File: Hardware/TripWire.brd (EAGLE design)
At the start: 32.3 x 50.2 mm, 69 parts, among them P1 LSP11, P2 LSP11, P3 LSP11, P4 LSP11, P5 LSP11, P6 LSP11, P7 LSP11, X1 GADGETEER-SOCKET

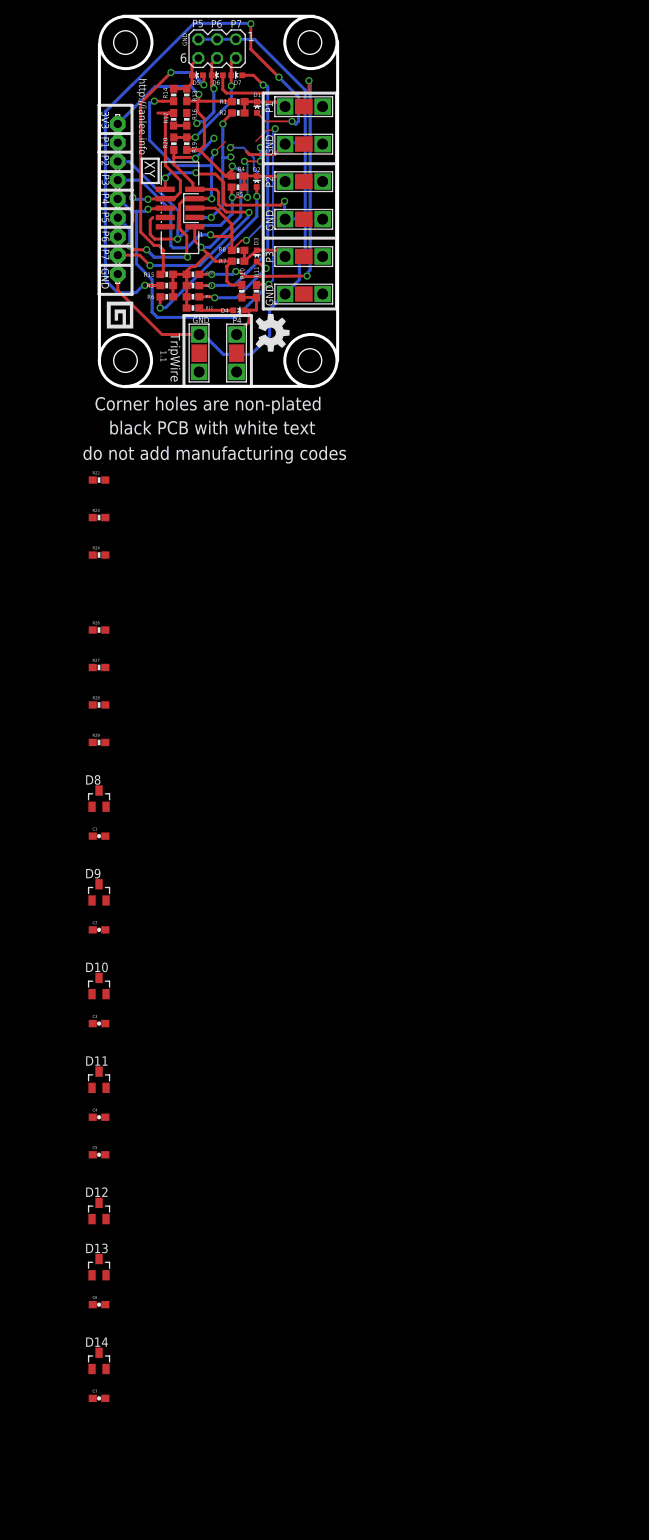
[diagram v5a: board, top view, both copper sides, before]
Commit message: Created BAT54SDW diode array part.
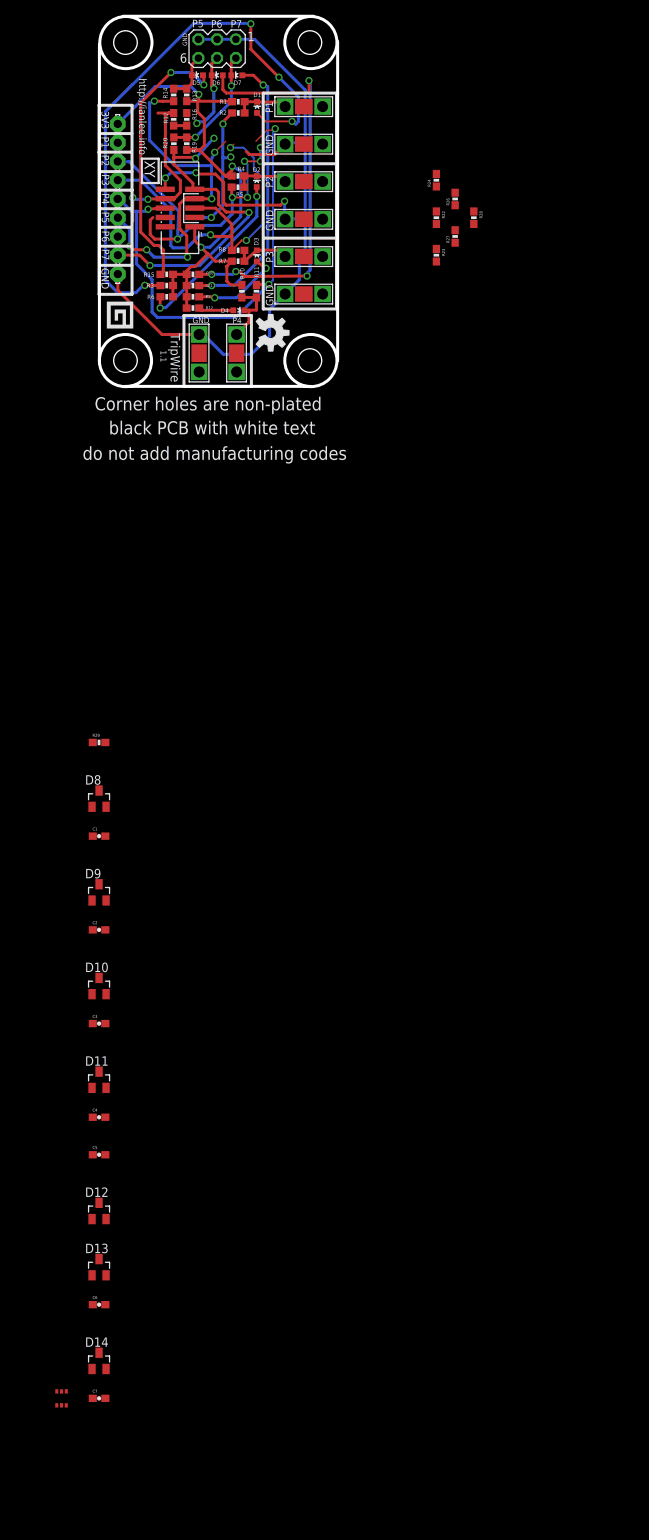
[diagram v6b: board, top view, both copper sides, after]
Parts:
- added U$9: BAT54SDW, SoftDust:SOT-363
- moved R28 83.3 mm to (50.8, 22.9), turned to 270 degrees
- moved R26 75.8 mm to (48.3, 25.4), turned to 90 degrees
- moved R27 75.8 mm to (48.3, 20.3), turned to 90 degrees
- moved R24 68.3 mm to (45.7, 27.9), turned to 90 degrees
- moved R22 57.9 mm to (45.7, 22.9), turned to 270 degrees
- moved R23 57.9 mm to (45.7, 17.8), turned to 270 degrees
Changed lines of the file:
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@@
 <?xml version="1.0" encoding="utf-8"?>
 <!DOCTYPE eagle SYSTEM "eagle.dtd">
-<eagle version="6.1">
+<eagle version="6.4">
 <drawing>
 <settings>
@@
 </class>
 </classes>
-<designrules>
+<designrules name="default">
 <description language="en">
 &lt;b&gt;EAGLE Design Rules&lt;/b&gt;
@@
 </element>
 <element name="LOGO1" library="SparkFun-Aesthetics" package="OSHW-LOGO-M" value="OSHW-LOGOM" x="23.2664" y="7.2644" rot="R270"/>
-<element name="R22" library="SparkFun-Resistors" package="0603-RES" value="10" x="0" y="-12.7"/>
-<element name="R23" library="SparkFun-Resistors" package="0603-RES" value="10" x="0" y="-17.78"/>
-<element name="R24" library="SparkFun-Resistors" package="0603-RES" value="10" x="0" y="-22.86"/>
-<element name="R26" library="SparkFun-Resistors" package="0603-RES" value="10" x="0" y="-33.02"/>
-<element name="R27" library="SparkFun-Resistors" package="0603-RES" value="10" x="0" y="-38.1"/>
-<element name="R28" library="SparkFun-Resistors" package="0603-RES" value="10" x="0" y="-43.18"/>
+<element name="R22" library="SparkFun-Resistors" package="0603-RES" value="10" x="45.72" y="22.86" rot="R270"/>
+<element name="R23" library="SparkFun-Resistors" package="0603-RES" value="10" x="45.72" y="17.78" rot="R270"/>
+<element name="R24" library="SparkFun-Resistors" package="0603-RES" value="10" x="45.72" y="27.94" rot="R90"/>
+<element name="R26" library="SparkFun-Resistors" package="0603-RES" value="10" x="48.26" y="25.4" rot="R90"/>
+<element name="R27" library="SparkFun-Resistors" package="0603-RES" value="10" x="48.26" y="20.32" rot="R90"/>
+<element name="R28" library="SparkFun-Resistors" package="0603-RES" value="10" x="50.8" y="22.86" rot="R270"/>
 <element name="R29" library="SparkFun-Resistors" package="0603-RES" value="10" x="0" y="-48.26"/>
 <element name="D8" library="diode" package="SOT23" value="BAT54S" x="0" y="-55.88"/>
@@
 <element name="D14" library="diode" package="SOT23" value="BAT54S" x="0" y="-132.08"/>
 <element name="C7" library="SparkFun-Capacitors" package="0603-CAP" value="0.01 uF" x="0" y="-137.16"/>
+<element name="U$9" library="SoftDust" package="SOT-363" value="BAT54SDW" x="-5.08" y="-137.16"/>
 </elements>
 <signals>
@@
 <contactref element="R26" pad="1"/>
 <contactref element="D8" pad="3"/>
-<wire x1="-0.85" y1="-33.02" x2="0" y2="-54.78" width="0" layer="19" extent="1-1"/>
-<wire x1="12.6734" y1="22.8854" x2="-0.85" y2="-33.02" width="0" layer="19" extent="1-16"/>
+<wire x1="48.26" y1="24.55" x2="0" y2="-54.78" width="0" layer="19" extent="1-1"/>
+<wire x1="12.6734" y1="22.8854" x2="48.26" y2="24.55" width="0" layer="19" extent="1-16"/>
 </signal>
 <signal name="PIN4">
@@
 <contactref element="R22" pad="2"/>
 <contactref element="D10" pad="3"/>
-<wire x1="0.85" y1="-12.7" x2="0" y2="-80.18" width="0" layer="19" extent="1-1"/>
-<wire x1="7.5438" y1="19.9644" x2="0.85" y2="-12.7" width="0" layer="19" extent="1-1"/>
+<wire x1="45.72" y1="22.01" x2="0" y2="-80.18" width="0" layer="19" extent="1-1"/>
+<wire x1="7.5438" y1="19.9644" x2="45.72" y2="22.01" width="0" layer="19" extent="1-1"/>
 </signal>
 <signal name="PIN5">
@@
 <contactref element="R27" pad="1"/>
 <contactref element="D9" pad="3"/>
-<wire x1="-0.85" y1="-38.1" x2="0" y2="-67.48" width="0" layer="19" extent="1-1"/>
-<wire x1="10.033" y1="18.7706" x2="-0.85" y2="-38.1" width="0" layer="19" extent="1-16"/>
+<wire x1="48.26" y1="19.47" x2="0" y2="-67.48" width="0" layer="19" extent="1-1"/>
+<wire x1="10.033" y1="18.7706" x2="48.26" y2="19.47" width="0" layer="19" extent="1-16"/>
 </signal>
 <signal name="PIN7">
@@
 <contactref element="R28" pad="1"/>
 <contactref element="D12" pad="3"/>
-<wire x1="-0.85" y1="-43.18" x2="0" y2="-110.66" width="0" layer="19" extent="1-1"/>
-<wire x1="12.9836" y1="25.4254" x2="-0.85" y2="-43.18" width="0" layer="19" extent="1-1"/>
+<wire x1="50.8" y1="23.71" x2="0" y2="-110.66" width="0" layer="19" extent="1-1"/>
+<wire x1="12.9836" y1="25.4254" x2="50.8" y2="23.71" width="0" layer="19" extent="1-1"/>
 </signal>
 <signal name="PIN9">
@@
 <contactref element="R23" pad="2"/>
 <contactref element="D11" pad="3"/>
-<wire x1="0.85" y1="-17.78" x2="0" y2="-92.88" width="0" layer="19" extent="1-1"/>
-<wire x1="7.8994" y1="9.3472" x2="0.85" y2="-17.78" width="0" layer="19" extent="1-16"/>
+<wire x1="45.72" y1="16.93" x2="0" y2="-92.88" width="0" layer="19" extent="1-1"/>
+<wire x1="7.8994" y1="9.3472" x2="45.72" y2="16.93" width="0" layer="19" extent="1-16"/>
 </signal>
 <signal name="PIN8">
@@
 <contactref element="R24" pad="2"/>
 <contactref element="D13" pad="3"/>
-<wire x1="0.85" y1="-22.86" x2="0" y2="-118.28" width="0" layer="19" extent="1-1"/>
-<wire x1="4.572" y1="22.324" x2="0.85" y2="-22.86" width="0" layer="19" extent="1-1"/>
+<wire x1="45.72" y1="28.79" x2="0" y2="-118.28" width="0" layer="19" extent="1-1"/>
+<wire x1="4.572" y1="22.324" x2="45.72" y2="28.79" width="0" layer="19" extent="1-1"/>
 </signal>
 <signal name="N$13">
@@
 <contactref element="R22" pad="1"/>
 <wire x1="2.5286" y1="30.4838" x2="8.9728" y2="22.8962" width="0" layer="19" extent="1-1"/>
-<wire x1="-0.85" y1="-12.7" x2="8.9728" y2="22.8962" width="0" layer="19" extent="1-1"/>
+<wire x1="45.72" y1="23.71" x2="8.9728" y2="22.8962" width="0" layer="19" extent="1-1"/>
 </signal>
 <signal name="N$16">
@@
 <contactref element="R23" pad="1"/>
 <wire x1="2.5248" y1="25.4038" x2="8.9728" y2="24.1662" width="0" layer="19" extent="1-1"/>
-<wire x1="-0.85" y1="-17.78" x2="8.9728" y2="24.1662" width="0" layer="19" extent="1-1"/>
+<wire x1="45.72" y1="18.63" x2="8.9728" y2="24.1662" width="0" layer="19" extent="1-1"/>
 </signal>
 <signal name="N$17">
@@
 <contactref element="R24" pad="1"/>
 <wire x1="2.5464" y1="20.2984" x2="8.9728" y2="25.4362" width="0" layer="19" extent="1-1"/>
-<wire x1="-0.85" y1="-22.86" x2="2.5464" y2="20.2984" width="0" layer="19" extent="1-1"/>
+<wire x1="45.72" y1="27.09" x2="2.5464" y2="20.2984" width="0" layer="19" extent="1-1"/>
 </signal>
 <signal name="N$18">
@@
 <contactref element="R26" pad="2"/>
 <wire x1="2.535" y1="33.0238" x2="12.9728" y2="22.8962" width="0" layer="19" extent="1-1"/>
-<wire x1="0.85" y1="-33.02" x2="12.9728" y2="22.8962" width="0" layer="19" extent="1-1"/>
+<wire x1="48.26" y1="26.25" x2="12.9728" y2="22.8962" width="0" layer="19" extent="1-1"/>
 </signal>
 <signal name="N$19">
@@
 <contactref element="P3" pad="MP"/>
 <contactref element="R27" pad="2"/>
-<wire x1="12.9728" y1="24.1662" x2="0.85" y2="-38.1" width="0" layer="19" extent="1-1"/>
+<wire x1="12.9728" y1="24.1662" x2="48.26" y2="21.17" width="0" layer="19" extent="1-1"/>
 <wire x1="2.5312" y1="27.9438" x2="12.9728" y2="24.1662" width="0" layer="19" extent="1-1"/>
 </signal>
@@
 <wire x1="11.644" y1="25.4362" x2="12.9728" y2="25.4362" width="0.4064" layer="1"/>
 <contactref element="R28" pad="2"/>
-<wire x1="7.4422" y1="17.526" x2="0.85" y2="-43.18" width="0" layer="19" extent="1-16"/>
+<wire x1="7.4422" y1="17.526" x2="50.8" y2="22.01" width="0" layer="19" extent="1-16"/>
 </signal>
 <signal name="N$21">
@@
 </board>
 </drawing>
+<compatibility>
+<note version="6.3" minversion="6.2.2" severity="warning">
+Since Version 6.2.2 text objects can contain more than one line,
+which will not be processed correctly with this version.
+</note>
+</compatibility>
 </eagle>

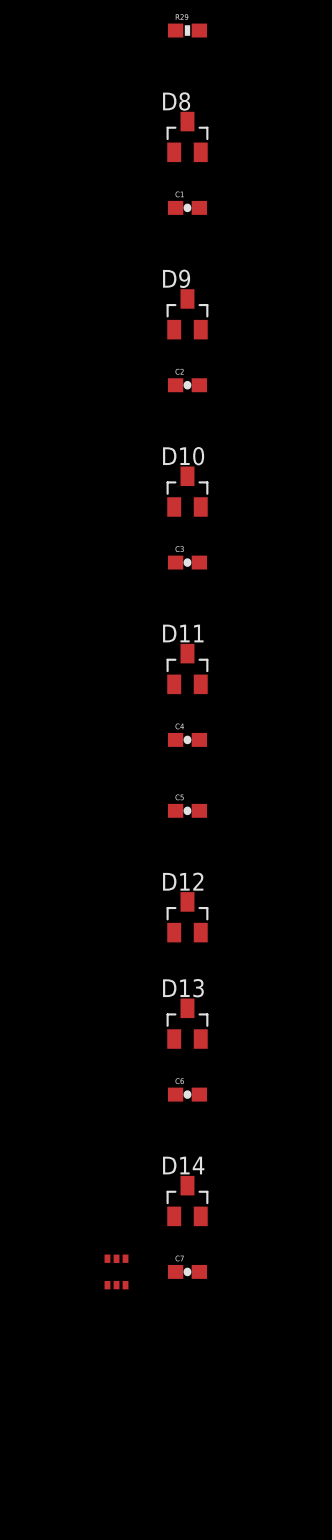
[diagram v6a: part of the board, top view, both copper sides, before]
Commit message: Replaced all transistor pairs with BAT54SDW diode arrays.
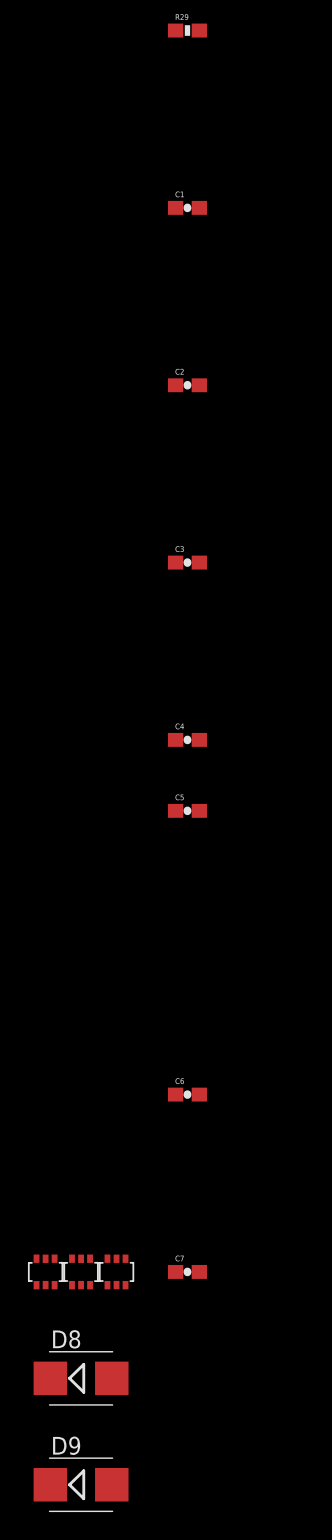
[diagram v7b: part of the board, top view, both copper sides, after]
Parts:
- removed D10, D11, D12, D13, D14: BAT54S, diode:SOT23
- added U$10, U$11: BAT54SDW, SoftDust:SOT-363
- D8, D9: value BAT54S -> (none); device diode:SOT23 -> diode:SMB
- moved D8 89.2 mm to (-7.62, -144.8)
- moved D9 84.2 mm to (-7.62, -152.4)
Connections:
- net 3V3: now also D9.C, U$10.P$1, U$10.P$4, U$11.P$1, U$11.P$4, U$9.P$1, U$9.P$4; no longer D10.2, D11.2, D12.2, D13.2, D14.2, D8.2, D9.2
- net GND: now also D8.A, U$10.P$2, U$10.P$3, U$11.P$2, U$11.P$3, U$9.P$2, U$9.P$3; no longer D10.1, D11.1, D12.1, D13.1, D14.1, D8.1, D9.1
- net PIN3: now also U$9.P$5; no longer D8.3
- net PIN4: now also U$9.P$0; no longer D10.3
- net PIN5: now also U$10.P$5; no longer D9.3
- net PIN6: now also U$10.P$0; no longer D11.3
- net PIN7: now also U$11.P$5; no longer D12.3
- net PIN8: now also U$11.P$0; no longer D13.3
- net PIN9: now also D8.C, D9.A; no longer D14.3

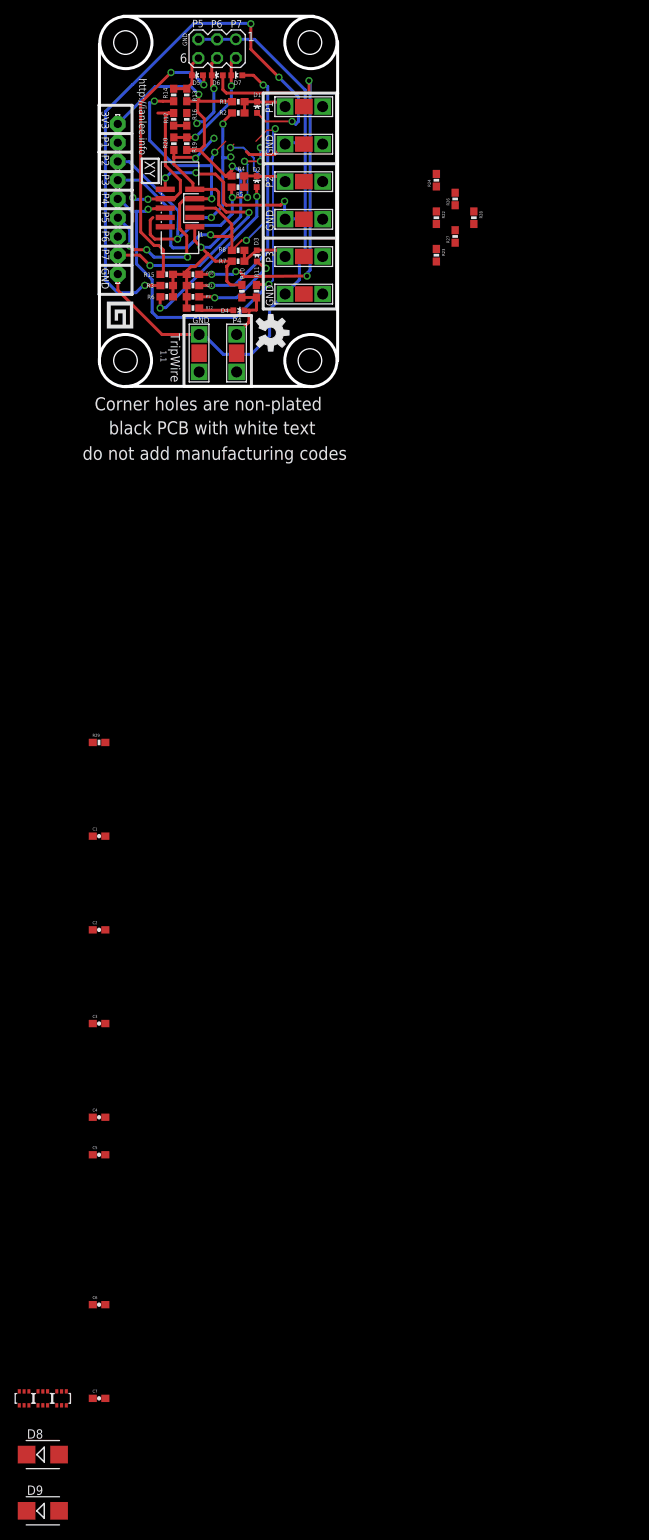
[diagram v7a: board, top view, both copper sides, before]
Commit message: Replaced single diodes with BAT42 custom part.
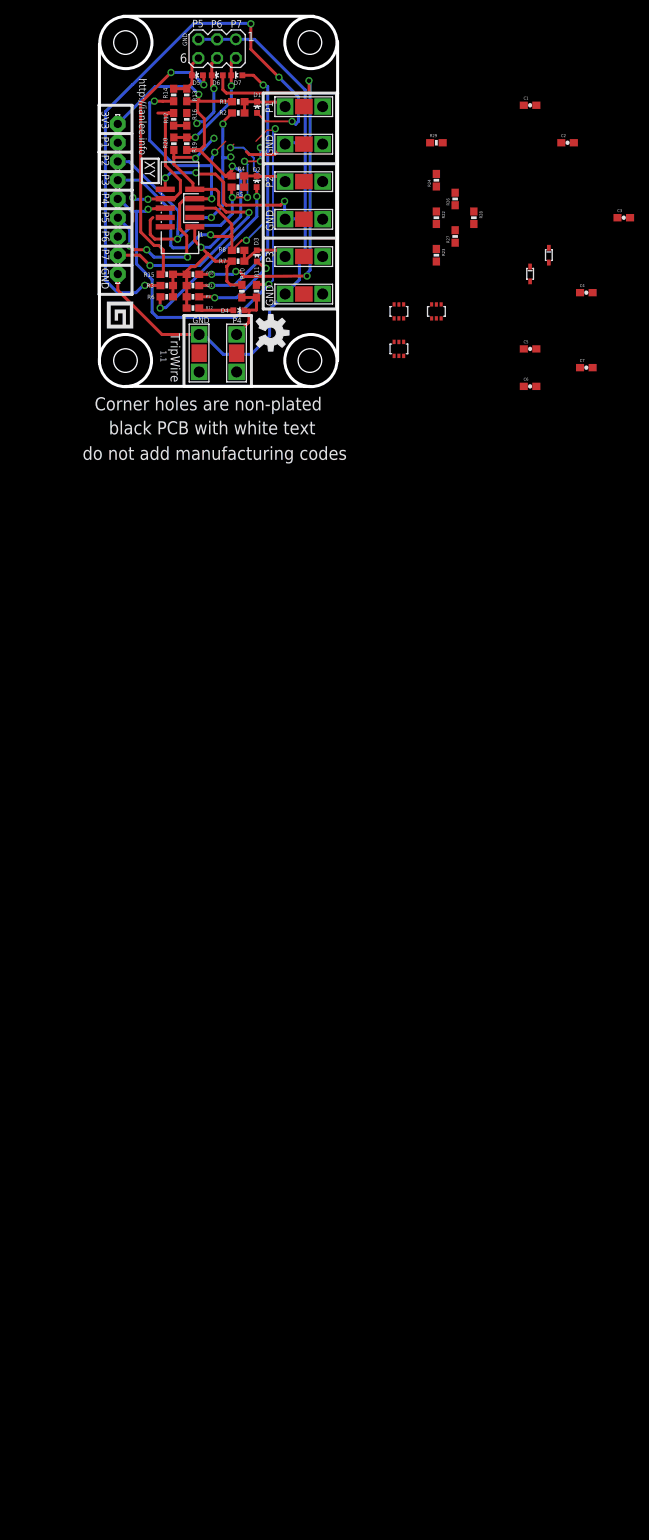
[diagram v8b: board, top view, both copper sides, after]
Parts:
- removed D8, D9: (no value), diode:SMB
- added U$12, U$13: BAT42-SCHOTTKY-DIODE, SoftDust:SOD-523F
- moved U$10 156.7 mm to (45.7, 10.2)
- moved U$11 155.8 mm to (40.6, 10.2)
- moved C7 154.5 mm to (66.0, 2.54)
- moved U$9 149.4 mm to (40.6, 5.08)
- moved C6 137.5 mm to (58.4, 0.00)
- moved C3 130.3 mm to (71.1, 22.9)
- moved C4 129.8 mm to (66.0, 12.7)
- moved C2 124.1 mm to (63.5, 33.0)
- moved C5 123.9 mm to (58.4, 5.08)
- moved C1 115.0 mm to (58.4, 38.1)
- moved R29 93.3 mm to (45.7, 33.0)
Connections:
- net 3V3: now also U$12.P$1; no longer D9.C
- net GND: now also U$13.P$2; no longer D8.A
- net PIN9: now also U$12.P$2, U$13.P$1; no longer D8.C, D9.A
